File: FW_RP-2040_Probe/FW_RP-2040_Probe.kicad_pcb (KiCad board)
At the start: 2 copper layers, 26 x 30 mm, 38 parts, among them P1 USB_C_Plug_USB2.0, P2 JST Female 1x3, P3 JST Female 1x3, U1 AP2112K-3.3, U2 RP2040, U3 W25Q128JVS, U4 MC74VHC1GT126, U5 MC74VHC1GT126, Y1 RH100-12.000-9-1015-TR-NS1

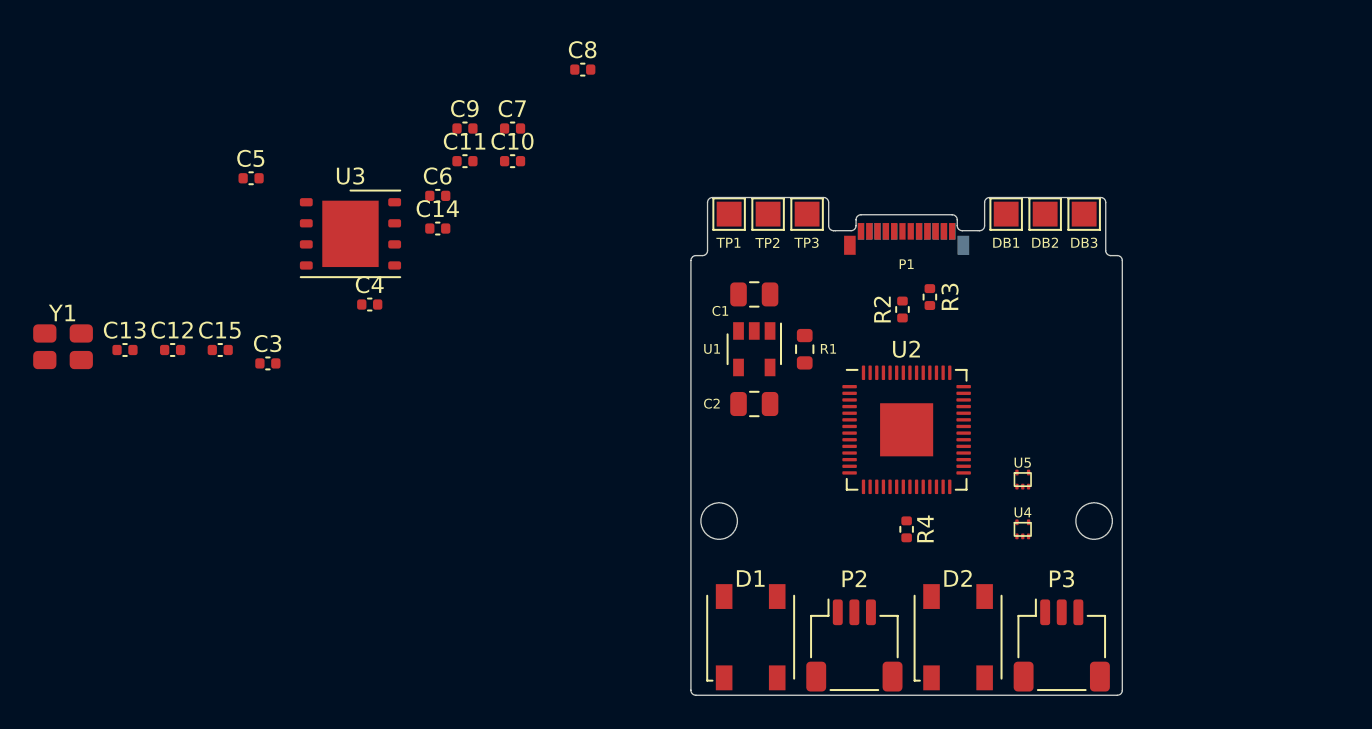
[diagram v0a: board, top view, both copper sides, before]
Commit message: Update schematic to pinout v1.1.1, update layout to v0.5.0
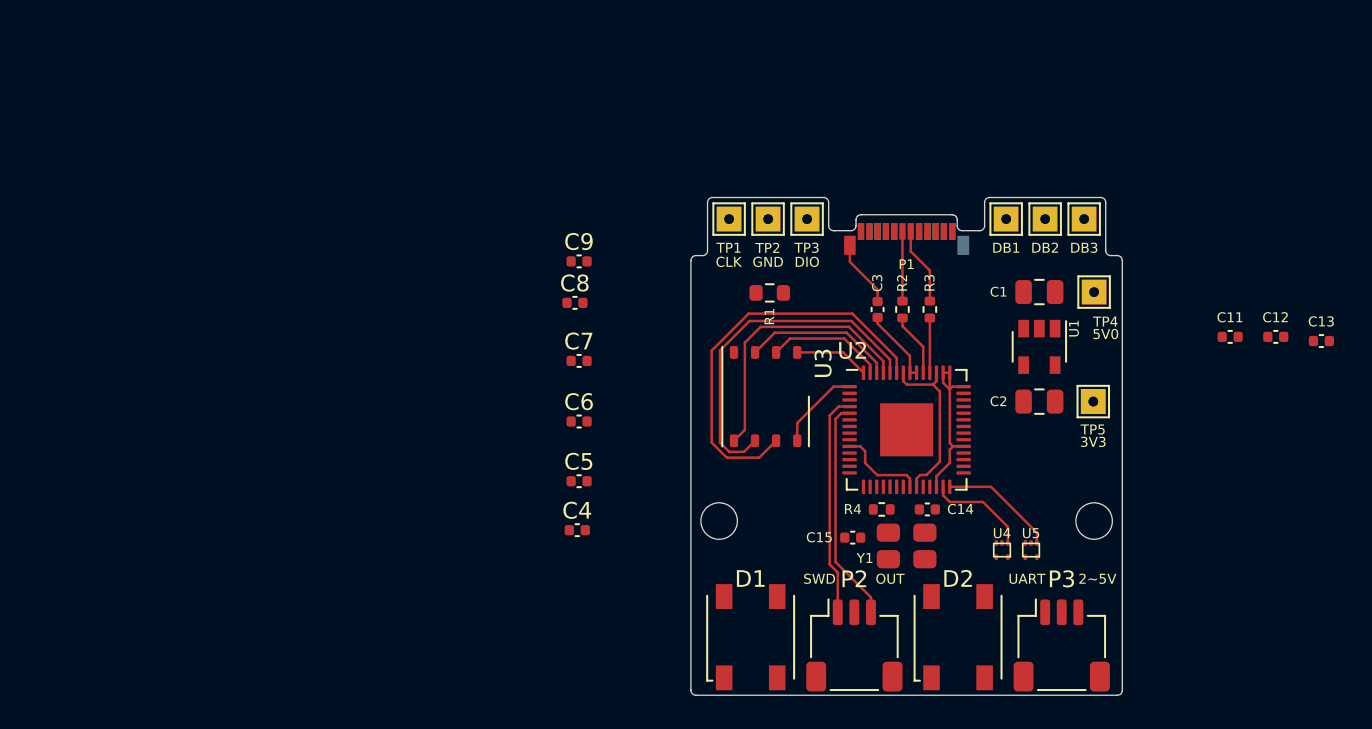
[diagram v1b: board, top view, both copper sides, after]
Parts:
- removed C10: 10nF, Capacitor_SMD:C_0402_1005Metric
- added TP4: TestPoint, KKicadLib:TestPoint_Pad_1.5x1.5mm_THT, F.Cu at (151.3, 132.7)
- added TP5: TestPoint, KKicadLib:TestPoint_Pad_1.5x1.5mm_THT, F.Cu at (151.2, 139.3)
- DB1, DB2, DB3, TP1, TP2, TP3: footprint TestPoint:TestPoint_Pad_1.5x1.5mm -> KKicadLib:TestPoint_Pad_1.5x1.5mm_THT
- moved C13 72.1 mm to (165.0, 135.7)
- moved C12 66.5 mm to (162.2, 135.4)
- moved Y1 52.2 mm to (140.0, 148.0)
- moved C11 47.3 mm to (159.5, 135.4)
- moved C15 39.8 mm to (136.8, 147.5), turned to 180 degrees
- moved C3 36.9 mm to (138.2, 133.8), turned to 90 degrees
- moved C14 34.0 mm to (141.2, 145.8)
- moved C5 26.9 mm to (120.3, 144.1)
- moved U3 26.9 mm to (131.5, 139.0), turned to -90 degrees
- moved C4 18.5 mm to (120.2, 147.1)
- moved C1 17.2 mm to (148.0, 132.7), turned to 0 degrees
- moved C2 17.2 mm to (148.0, 139.3), turned to 0 degrees
- moved U1 17.2 mm to (148.0, 136.0)
- moved C6 16.0 mm to (120.3, 140.5)
- moved C7 14.6 mm to (120.3, 136.8)
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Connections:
- U2 pad 1: Net-(U2-Pad1) -> +3V3
- U2 pad 10: Net-(U2-Pad1) -> +3V3
- U2 pad 2: /UART_TX -> /LED1
- U2 pad 22: Net-(U2-Pad1) -> +3V3
- U2 pad 23: Net-(U2-Pad23) -> +1V1
- U2 pad 26: unconnected-(U2-Pad26) -> +3V3
- U2 pad 27: unconnected-(U2-Pad27) -> /UART_TX
- U2 pad 28: unconnected-(U2-Pad28) -> /UART_RX
- U2 pad 29: unconnected-(U2-Pad29) -> /DEBUG1
- U2 pad 3: /UART_RX -> /LED2
- U2 pad 30: unconnected-(U2-Pad30) -> /DEBUG2
- U2 pad 31: unconnected-(U2-Pad31) -> /DEBUG3
- U2 pad 33: Net-(U2-Pad1) -> +3V3
- U2 pad 42: Net-(U2-Pad1) -> +3V3
- U2 pad 43: unconnected-(U2-Pad43) -> +3V3
- U2 pad 45: unconnected-(U2-Pad45) -> +1V1
- U2 pad 48: unconnected-(U2-Pad48) -> +3V3
- U2 pad 49: Net-(U2-Pad1) -> +3V3
- U2 pad 50: Net-(U2-Pad23) -> +1V1
- U2 pad 6: /LED1 -> unconnected-(U2-Pad6)
- U2 pad 7: /LED2 -> unconnected-(U2-Pad7)
- Y1 pad 2: /YI -> (no net)
- Y1 pad 3: (no net) -> /YI
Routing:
- net +3V3: track 0.00 -> 25.5 mm
- net /MEM_D3: track 0.00 -> 24.3 mm
- net /MEM_CLK: track 0.00 -> 20.9 mm
- net /MEM_D0: track 0.00 -> 16.5 mm
- net /SWDIO_OUT: track 0.00 -> 13.5 mm
- net /SWCLK_OUT: track 0.00 -> 13.5 mm
- net +1V1: track 0.00 -> 10.3 mm
- net /MEM_D2: track 0.00 -> 9.18 mm
- net /MEM_D1: track 0.00 -> 7.16 mm
- net /UART_RX: track 0.00 -> 7.02 mm
- net /UART_TX: track 0.00 -> 6.17 mm
- net /USB_N: track 0.00 -> 4.68 mm
- net /MEM_CS_N: track 0.00 -> 4.50 mm
- net /USB_P: track 0.00 -> 4.20 mm
- net GND: track 0.00 -> 4.08 mm
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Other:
- board text added: "2~5V"
- board text added: "3V3"
- board text added: "5V0"
- board text added: "CLK"
- board text added: "DIO"
- board text added: "GND"
- board text added: "OUT"
- board text added: "SWD"
- board text added: "UART"

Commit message: Add v1.1.1 schematic and PCB
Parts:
- removed C12, C13: 10nF, Capacitor_SMD:C_0402_1005Metric
- R1: footprint Resistor_SMD:R_0603_1608Metric -> Resistor_SMD:R_0402_1005Metric
- moved C4 27.2 mm to (144.2, 134.5), turned to 90 degrees
- moved C5 25.8 mm to (146.0, 142.0)
- moved C6 24.0 mm to (143.2, 147.4), turned to -90 degrees
- moved C7 18.0 mm to (135.9, 145.8), turned to 90 degrees
- moved C8 17.1 mm to (133.4, 144.1), turned to -90 degrees
- moved C11 16.7 mm to (142.9, 134.0), turned to 90 degrees
- moved C9 16.3 mm to (135.0, 137.8), turned to 90 degrees
- moved R1 6.79 mm to (138.5, 133.5), turned to -90 degrees
- moved DB1 4.70 mm to (150.7, 128.3)
- moved DB3 4.70 mm to (146.0, 128.3)
- moved C3 1.12 mm to (137.2, 133.2)
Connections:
- C7 pad 1: +3V3 -> GND
- C7 pad 2: GND -> +3V3
- D1 pad 3: +3V3 -> VBUS
- D2 pad 3: +3V3 -> VBUS
- U2 pad 15: unconnected-(U2-Pad15) -> /LED2
- U2 pad 3: /LED2 -> unconnected-(U2-Pad3)
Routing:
- net GND: track 4.08 -> 84.5 mm, vias 0 -> 16
- net +3V3: track 25.5 -> 83.5 mm, vias 0 -> 2
- net VBUS: track 0.31 -> 54.9 mm, vias 0 -> 2
- net /SWCLK_IN: track 0.00 -> 22.1 mm, vias 0 -> 1
- net /SWDIO_IN: track 0.00 -> 20.8 mm, vias 0 -> 1
- net /DEBUG1: track 0.00 -> 20.5 mm, vias 0 -> 1
- net /LED1: track 0.00 -> 19.3 mm
- net /DEBUG2: track 0.00 -> 18.4 mm, vias 0 -> 1
- net /DEBUG3: track 0.00 -> 18.0 mm, vias 0 -> 1
- net /LED2: track 0.00 -> 17.1 mm
- net +1V1: track 10.3 -> 16.0 mm
- net /UART_RX_OUT: track 0.00 -> 5.08 mm
- net /YI: track 0.00 -> 4.64 mm
- net /UART_TX_OUT: track 0.00 -> 4.55 mm
- net /YO: track 0.00 -> 4.36 mm
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- added copper zone on B.Cu, net GND
